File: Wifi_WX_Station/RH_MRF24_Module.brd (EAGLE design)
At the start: 23.2 x 33.6 mm, 7 parts, among them M1 MRF24WB0MA

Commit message: updated BOM with all prices- As Checked in to BATCH PCB
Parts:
- moved R1 32.1 mm to (8.26, 19.1)
- moved JP1 31.9 mm to (14.0, 5.08), flipped to the bottom, turned to 270 degrees
- moved M1 31.8 mm to (24.1, 40.6)
- moved C2 31.8 mm to (19.7, 23.5)
- moved C3 31.8 mm to (14.0, 25.4)
- moved R2 31.8 mm to (17.1, 23.5)
- moved C1 28.8 mm to (7.62, 13.3)
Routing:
- net GND: track 99.1 -> 106.8 mm
- net RESET_: track 29.0 -> 33.3 mm
- net INT_: track 28.5 -> 25.2 mm
- net SDI: track 25.5 -> 22.2 mm
- net SDO: track 19.7 -> 22.8 mm
- net SCK: track 19.7 -> 22.8 mm
- net CS_: track 35.5 -> 32.4 mm
- net HIBER: track 36.7 -> 33.7 mm
- net +3V3: track 64.1 -> 65.5 mm
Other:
- board text removed: "0.5080 mm / 20.000 mil"
- board text removed: "0.6000 mm / 23.622 mil"
- board text removed: "0.8890 mm / 35.000 mil"
- board text removed: "1 different diameters with default symbols! (10 drills)"
- board text removed: "Date: 1/27/2013 12:40:03 PM"
- board text removed: "Drill legend"

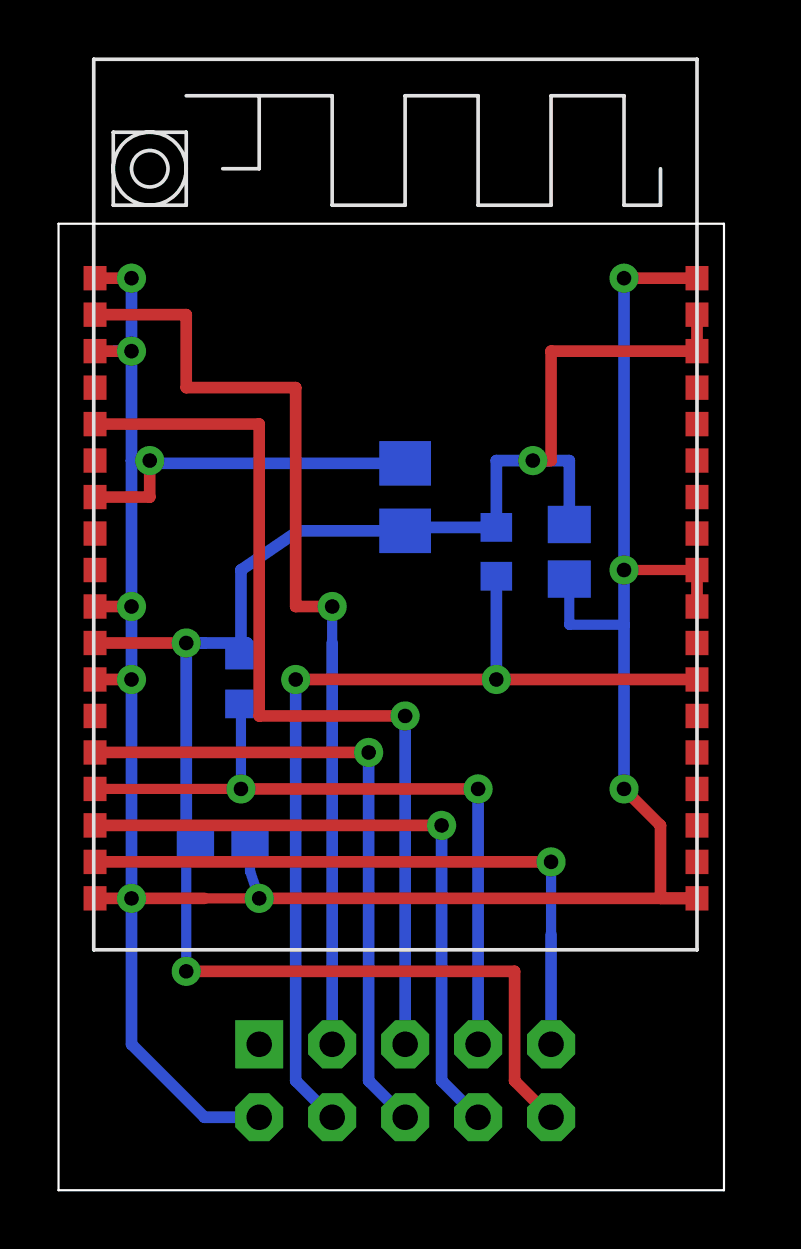
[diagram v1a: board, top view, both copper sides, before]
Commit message: added SILabs Hygrometer board Added frames to the schematics
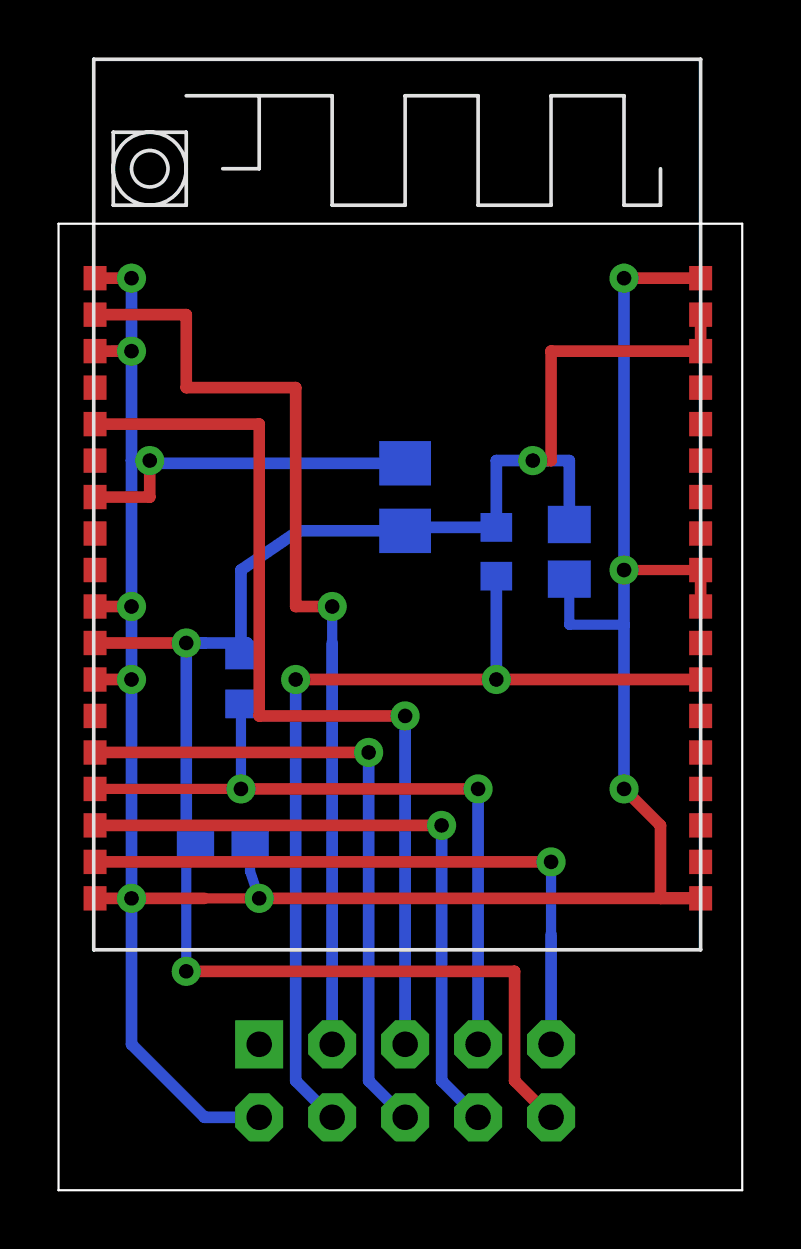
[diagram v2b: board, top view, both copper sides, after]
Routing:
- net GND: track 106.8 -> 107.3 mm
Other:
- board size 23.2 x 33.6 mm -> 23.8 x 33.6 mm
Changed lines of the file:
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@@
 <setting verticaltext="up"/>
 </settings>
-<grid distance="0.05" unitdist="inch" unit="inch" style="lines" multiple="1" display="no" altdistance="0.025" altunitdist="inch" altunit="inch"/>
+<grid distance="0.05" unitdist="inch" unit="inch" style="lines" multiple="1" display="yes" altdistance="0.025" altunitdist="inch" altunit="inch"/>
 <layers>
 <layer number="1" name="Top" color="4" fill="1" visible="yes" active="yes"/>
@@
 <layer number="27" name="tValues" color="7" fill="1" visible="yes" active="yes"/>
 <layer number="28" name="bValues" color="7" fill="1" visible="yes" active="yes"/>
-<layer number="29" name="tStop" color="7" fill="3" visible="no" active="yes"/>
-<layer number="30" name="bStop" color="7" fill="6" visible="no" active="yes"/>
+<layer number="29" name="tStop" color="7" fill="3" visible="yes" active="yes"/>
+<layer number="30" name="bStop" color="7" fill="6" visible="yes" active="yes"/>
 <layer number="31" name="tCream" color="7" fill="4" visible="yes" active="yes"/>
 <layer number="32" name="bCream" color="7" fill="5" visible="yes" active="yes"/>
@@
 <layer number="35" name="tGlue" color="7" fill="4" visible="yes" active="yes"/>
 <layer number="36" name="bGlue" color="7" fill="5" visible="yes" active="yes"/>
+<layer number="37" name="tTest" color="7" fill="1" visible="yes" active="yes"/>
+<layer number="38" name="bTest" color="7" fill="1" visible="yes" active="yes"/>
 <layer number="39" name="tKeepout" color="4" fill="11" visible="yes" active="yes"/>
 <layer number="40" name="bKeepout" color="1" fill="11" visible="yes" active="yes"/>
@@
 <layer number="97" name="Info" color="7" fill="1" visible="no" active="no"/>
 <layer number="98" name="Guide" color="6" fill="1" visible="no" active="no"/>
+<layer number="100" name="Moduls" color="14" fill="0" visible="yes" active="yes"/>
+<layer number="101" name="Flex-Kleb" color="1" fill="7" visible="yes" active="yes"/>
 <layer number="104" name="Name" color="16" fill="1" visible="yes" active="yes"/>
+<layer number="105" name="Beschreib" color="9" fill="1" visible="yes" active="yes"/>
+<layer number="106" name="BGA-Top" color="4" fill="1" visible="yes" active="yes"/>
+<layer number="107" name="BD-Top" color="5" fill="1" visible="yes" active="yes"/>
 <layer number="116" name="Patch_BOT" color="9" fill="4" visible="yes" active="yes"/>
 <layer number="121" name="_tsilk" color="7" fill="1" visible="yes" active="yes"/>
@@
 <board>
 <plain>
-<wire x1="1.905" y1="1.27" x2="25.07" y2="1.27" width="0.0762" layer="20"/>
-<wire x1="25.07" y1="1.27" x2="25.07" y2="34.915" width="0.0762" layer="20"/>
-<wire x1="25.07" y1="34.915" x2="1.905" y2="34.915" width="0.0762" layer="20"/>
+<wire x1="1.905" y1="1.27" x2="25.705" y2="1.27" width="0.0762" layer="20"/>
+<wire x1="25.705" y1="1.27" x2="25.705" y2="34.915" width="0.0762" layer="20"/>
+<wire x1="25.705" y1="34.915" x2="1.905" y2="34.915" width="0.0762" layer="20"/>
 <wire x1="1.905" y1="34.915" x2="1.905" y2="1.27" width="0.0762" layer="20"/>
 <text x="24.13" y="33.02" size="1.4224" layer="26" font="vector" rot="MR270">RV Builders Product 2013</text>
@@
 <contactref element="M1" pad="21"/>
 <wire x1="6.985" y1="11.43" x2="4.445" y2="11.43" width="0.4064" layer="1"/>
-<wire x1="24.13" y1="22.86" x2="24.13" y2="21.59" width="0.4064" layer="1"/>
+<wire x1="24.257" y1="22.86" x2="24.257" y2="21.59" width="0.4064" layer="1"/>
 <wire x1="3.175" y1="25.4" x2="5.08" y2="25.4" width="0.4064" layer="1"/>
 <wire x1="5.08" y1="25.4" x2="5.08" y2="26.67" width="0.4064" layer="1"/>
 <via x="5.08" y="26.67" extent="1-16" drill="0.508"/>
 <wire x1="6.985" y1="11.43" x2="8.89" y2="11.43" width="0.3556" layer="1"/>
-<wire x1="8.89" y1="11.43" x2="24.13" y2="11.43" width="0.4064" layer="1"/>
-<wire x1="24.13" y1="22.86" x2="21.59" y2="22.86" width="0.3556" layer="1"/>
+<wire x1="8.89" y1="11.43" x2="24.257" y2="11.43" width="0.4064" layer="1"/>
+<wire x1="24.257" y1="22.86" x2="21.59" y2="22.86" width="0.3556" layer="1"/>
 <via x="21.59" y="22.86" extent="1-16" drill="0.508"/>
 <wire x1="21.59" y1="20.955" x2="19.685" y2="20.955" width="0.3556" layer="16"/>
@@
 <wire x1="8.57" y1="12.38" x2="8.89" y2="11.43" width="0.3556" layer="16"/>
 <via x="8.89" y="11.43" extent="1-16" drill="0.508"/>
-<wire x1="24.13" y1="33.02" x2="21.59" y2="33.02" width="0.4064" layer="1"/>
+<wire x1="24.257" y1="33.02" x2="21.59" y2="33.02" width="0.4064" layer="1"/>
 <via x="21.59" y="33.02" extent="1-16" drill="0.508"/>
 <wire x1="21.59" y1="33.02" x2="21.59" y2="22.86" width="0.4064" layer="16"/>
-<wire x1="24.13" y1="11.43" x2="22.86" y2="11.43" width="0.4064" layer="1"/>
+<wire x1="24.257" y1="11.43" x2="22.86" y2="11.43" width="0.4064" layer="1"/>
 <wire x1="22.86" y1="11.43" x2="22.86" y2="13.97" width="0.4064" layer="1"/>
 <wire x1="22.86" y1="13.97" x2="21.59" y2="15.24" width="0.4064" layer="1"/>
@@
 <wire x1="18.415" y1="26.67" x2="19.05" y2="26.67" width="0.4064" layer="1"/>
 <wire x1="19.05" y1="26.67" x2="19.05" y2="30.48" width="0.4064" layer="1"/>
-<wire x1="19.05" y1="30.48" x2="24.13" y2="30.48" width="0.4064" layer="1"/>
-<wire x1="24.13" y1="30.48" x2="24.13" y2="31.75" width="0.4064" layer="1"/>
+<wire x1="19.05" y1="30.48" x2="24.257" y2="30.48" width="0.4064" layer="1"/>
+<wire x1="24.257" y1="30.48" x2="24.257" y2="31.75" width="0.4064" layer="1"/>
 <via x="18.415" y="26.67" extent="1-16" drill="0.508"/>
 <wire x1="17.78" y1="8.89" x2="6.35" y2="8.89" width="0.4064" layer="1"/>
@@
 <contactref element="JP1" pad="4"/>
 <via x="17.145" y="19.05" extent="1-16" drill="0.508"/>
-<wire x1="24.13" y1="19.05" x2="17.145" y2="19.05" width="0.4064" layer="1"/>
+<wire x1="24.257" y1="19.05" x2="17.145" y2="19.05" width="0.4064" layer="1"/>
 <via x="10.16" y="19.05" extent="1-16" drill="0.508"/>
 <wire x1="17.145" y1="19.05" x2="10.16" y2="19.05" width="0.4064" layer="1"/>
